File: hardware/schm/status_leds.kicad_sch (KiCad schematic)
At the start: 16 parts, among them J1 VBUS input fly-leads, U2 AP63205WU-7

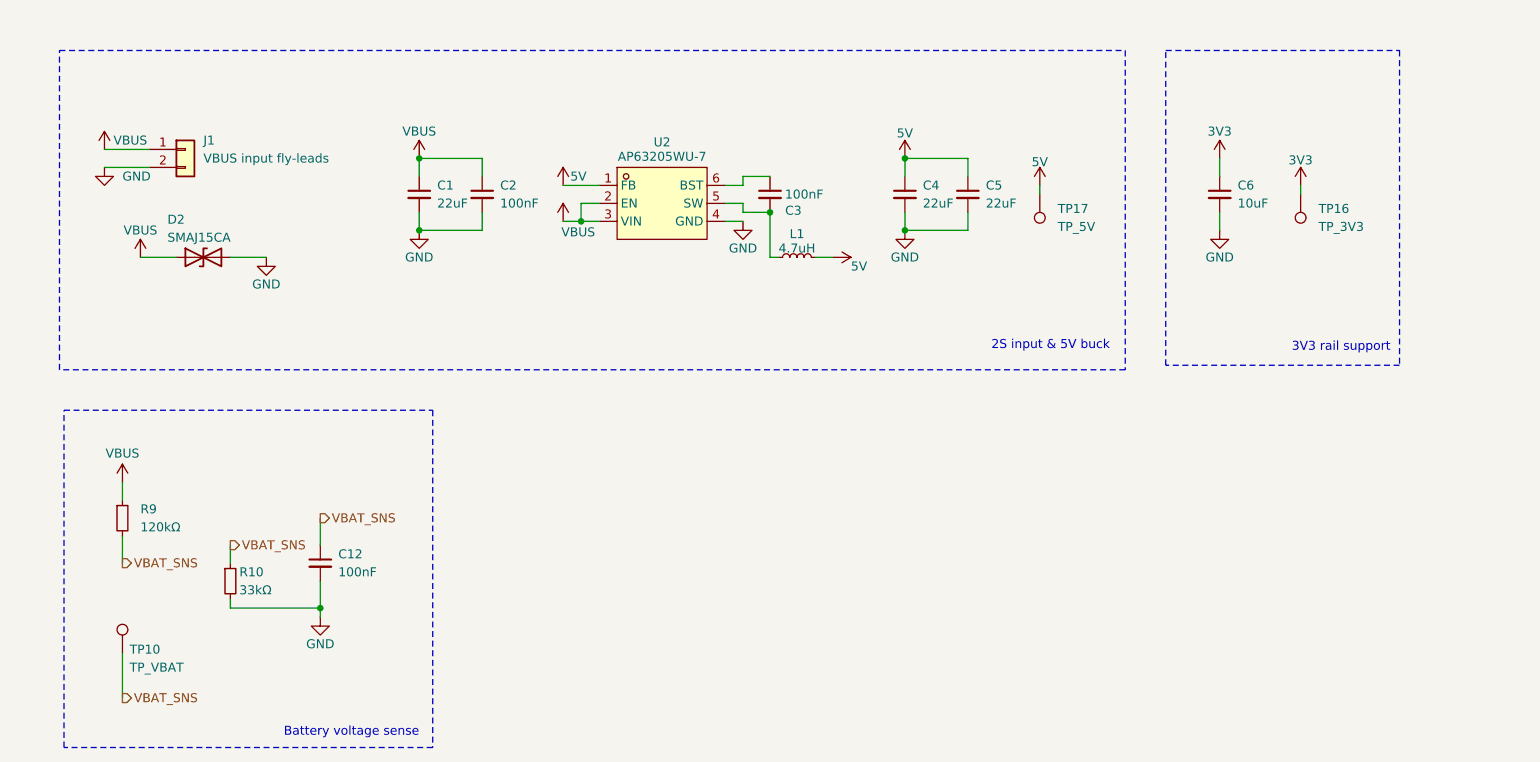
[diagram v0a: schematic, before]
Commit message: feat: organize into hierarchical sheets
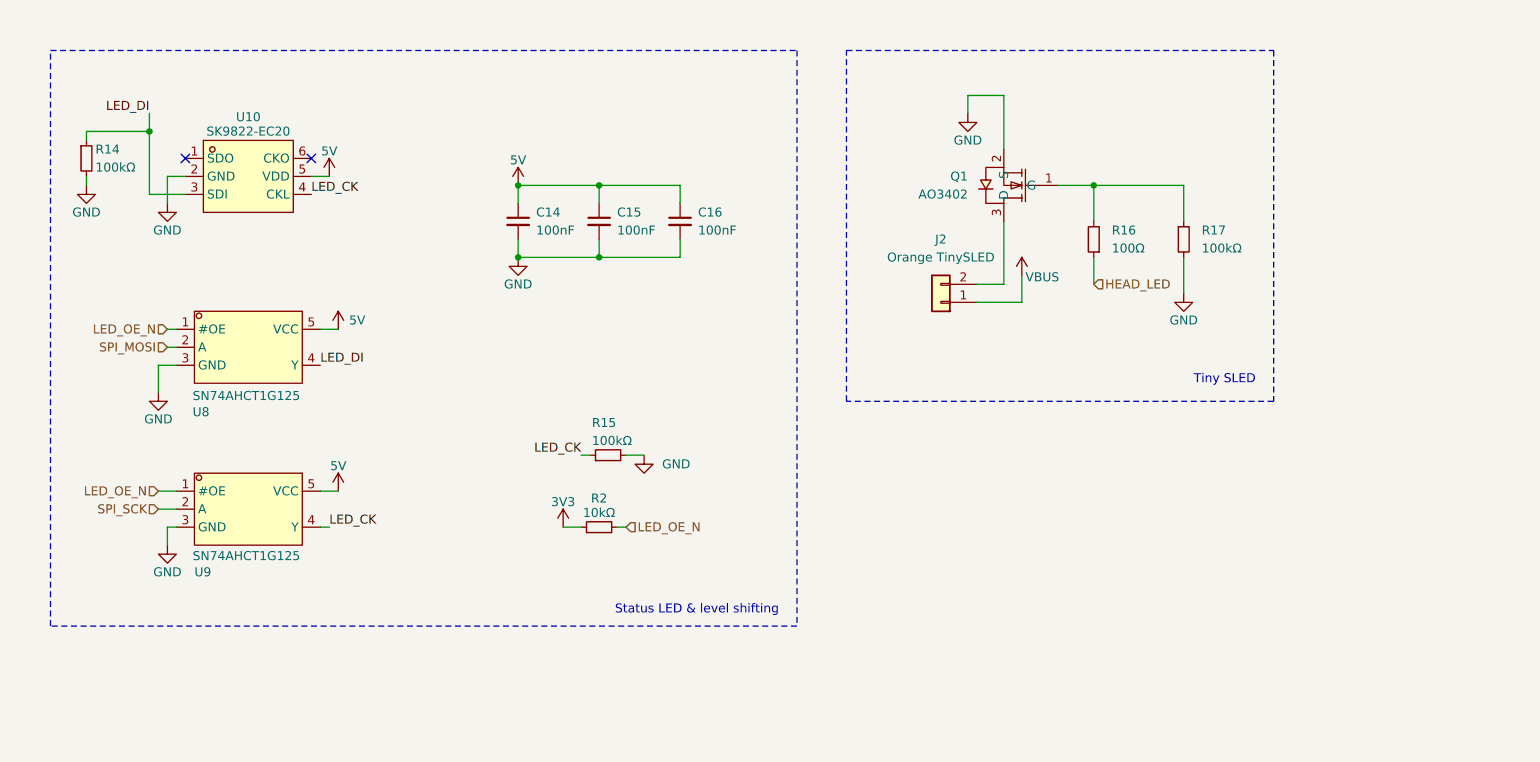
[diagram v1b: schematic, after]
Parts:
- removed C1, C4, C5: 22uF, Capacitor_SMD:C_0805_2012Metric, symbol Device:C_Small
- removed C12, C2, C3: 100nF, Capacitor_SMD:C_0402_1005Metric, symbol Device:C_Small
- removed C6: 10uF, Capacitor_SMD:C_0603_1608Metric, symbol Device:C_Small
- removed D2: SMAJ15CA, Diode_SMD:D_SMA, symbol Device:D_TVS
- removed J1: VBUS input fly-leads, Connector_Wire:SolderWire-0.5sqmm_1x02_P4.6mm_D0.9mm_OD2.1mm_Relief, symbol Connector_Generic:Conn_01x02
- removed L1: 4.7uH, Inductor_SMD:L_Wuerth_MAPI-4020, symbol Device:L_Small
- removed R10: 33kΩ, Resistor_SMD:R_0402_1005Metric, symbol Device:R_Small
- removed R9: 120kΩ, Resistor_SMD:R_0402_1005Metric, symbol Device:R_Small
- removed TP10: TP_VBAT, TestPoint:TestPoint_Pad_D1.0mm, symbol Connector:TestPoint
- removed TP16: TP_3V3, TestPoint:TestPoint_Pad_D1.0mm, symbol Connector:TestPoint
- removed TP17: TP_5V, TestPoint:TestPoint_Pad_D1.0mm, symbol Connector:TestPoint
- removed U2: AP63205WU-7, Library:TSOT-23-6_L2.9-W1.6-P0.95-LS2.8-BL, symbol Library:AP63205WU-7
- added C14, C15, C16: 100nF, Capacitor_SMD:C_0402_1005Metric, symbol Device:C_Small
- added J2: Orange TinySLED, Connector_Wire:SolderWire-0.25sqmm_1x02_P4.2mm_D0.65mm_OD1.7mm_Relief, symbol Connector_Generic:Conn_01x02
- added Q1: AO3402, Library:SOT-23_L2.9-W1.3-P1.90-LS2.4-BR, symbol Library:AO3402_C14385
- added R14, R15, R17: 100kΩ, Resistor_SMD:R_0402_1005Metric, symbol Device:R_Small
- added R16: 100Ω, Resistor_SMD:R_0402_1005Metric, symbol Device:R_Small
- added R2: 10kΩ, Resistor_SMD:R_0402_1005Metric, symbol Device:R_Small
- added U10: SK9822-EC20, Library:LED-SMD_6P-L2.0-W2.0-P0.80-TL, symbol Library:SK9822-EC20
- added U8, U9: SN74AHCT1G125, Library:SC-70-5_L2.0-W1.3-P0.65-LS2.1-BL, symbol Library:SN74AHCT1G125DCKR
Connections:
- net 3V3: now also R2.1
- net 5V: now also C14.1, C15.1, C16.1, U10.5 (VDD), U8.5 (VCC), U9.5 (VCC)
- net GND: now also C14.2, C15.2, C16.2, Q1.2 (S), R14.2, R15.2, R17.2, U10.2 (GND), U8.3 (GND), U9.3 (GND)
- net VBUS: now also J2.1 (Pin_1)
- new net: Q1.1 (G), R16.2, R17.1
- new net: J2.2 (Pin_2), Q1.3 (D)
- new net HEAD_LED: R16.1
- new net LED_CK: R15.1, U10.4 (CKL), U9.4 (Y)
- new net LED_DI: R14.1, U10.3 (SDI), U8.4 (Y)
- new net LED_OE_N: R2.2, U8.1 (#OE), U9.1 (#OE)
- new net SPI_MOSI: U8.2 (A)
- new net SPI_SCK: U9.2 (A)
- no-connect marks 0 -> 2
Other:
- note added: "Status LED & level shifting"
- note added: "Tiny SLED"
- note removed: "2S input & 5V buck"
- note removed: "3V3 rail support"
- note removed: "Battery voltage sense"

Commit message: feat: organize subsheets
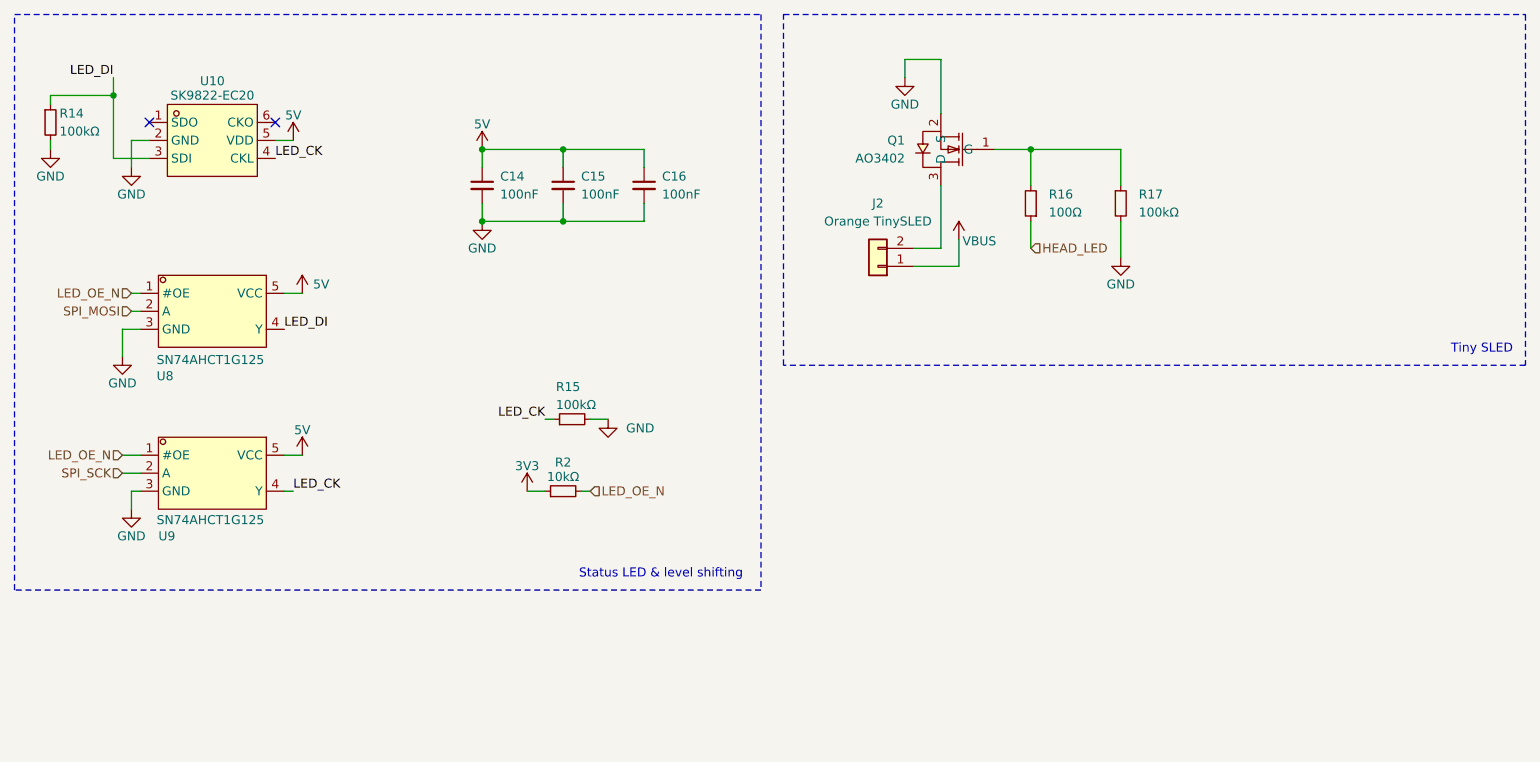
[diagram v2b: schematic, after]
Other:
- company: (none) -> Kieran Klukas
- title: (none) -> Holy Guacamole
- moved on the sheet: C14, C15, C16, J2, Q1, R14, R15, R16, R17, R2, U10, U8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
